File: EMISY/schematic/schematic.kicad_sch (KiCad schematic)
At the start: 6 parts

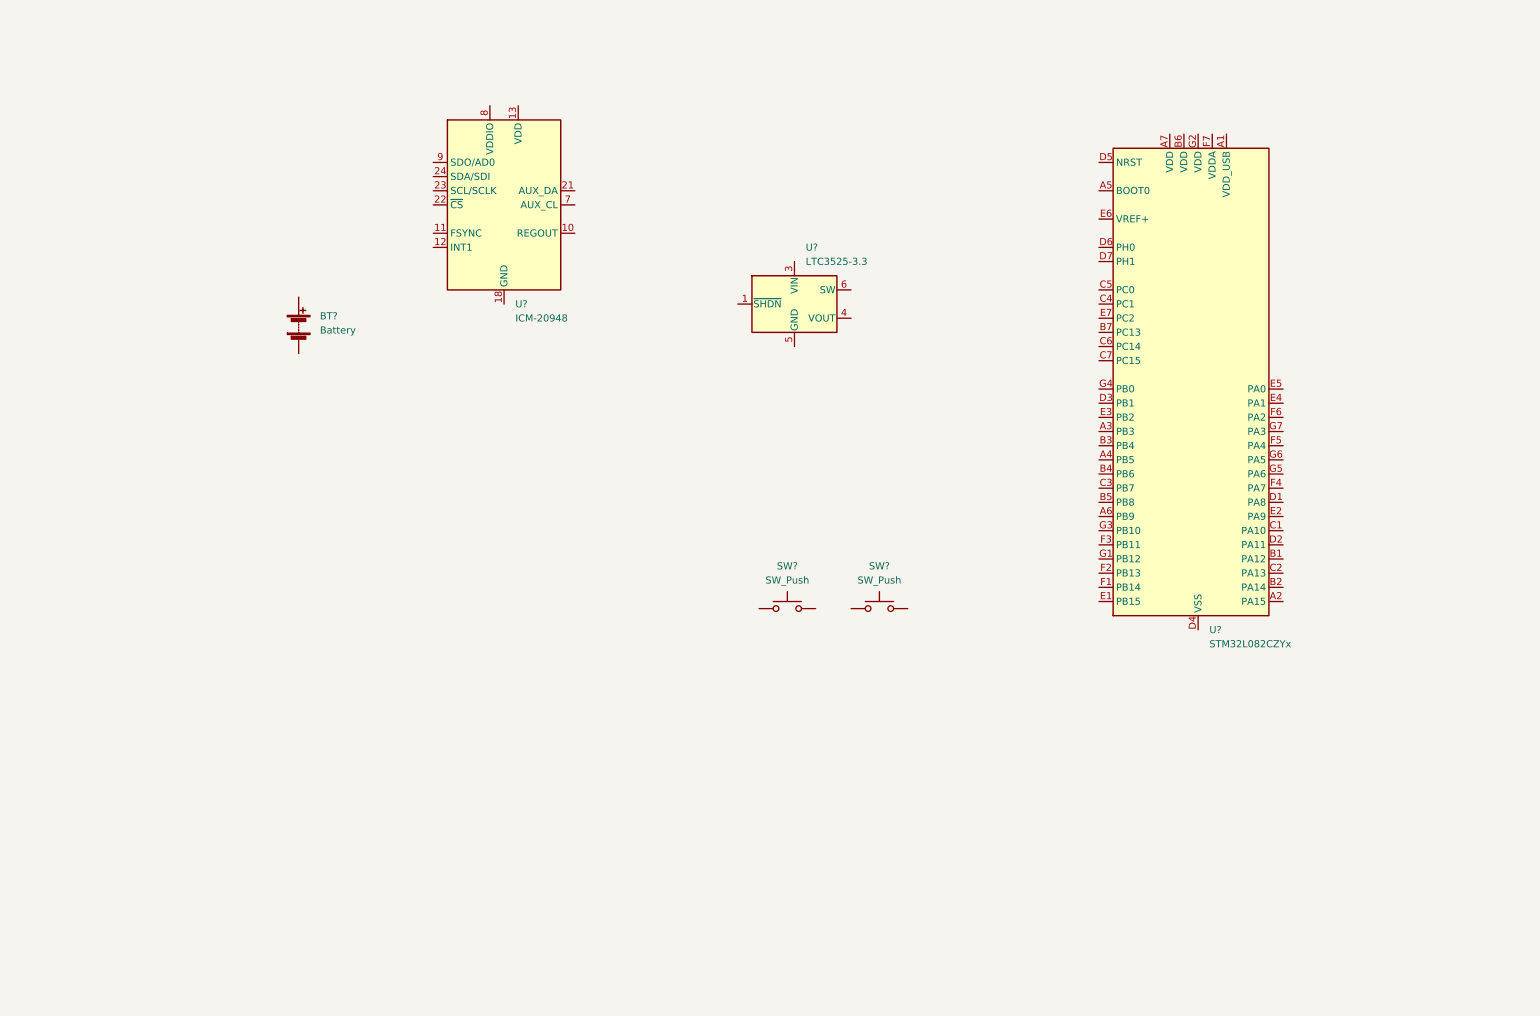
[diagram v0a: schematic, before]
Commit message: feat: add magnetometer
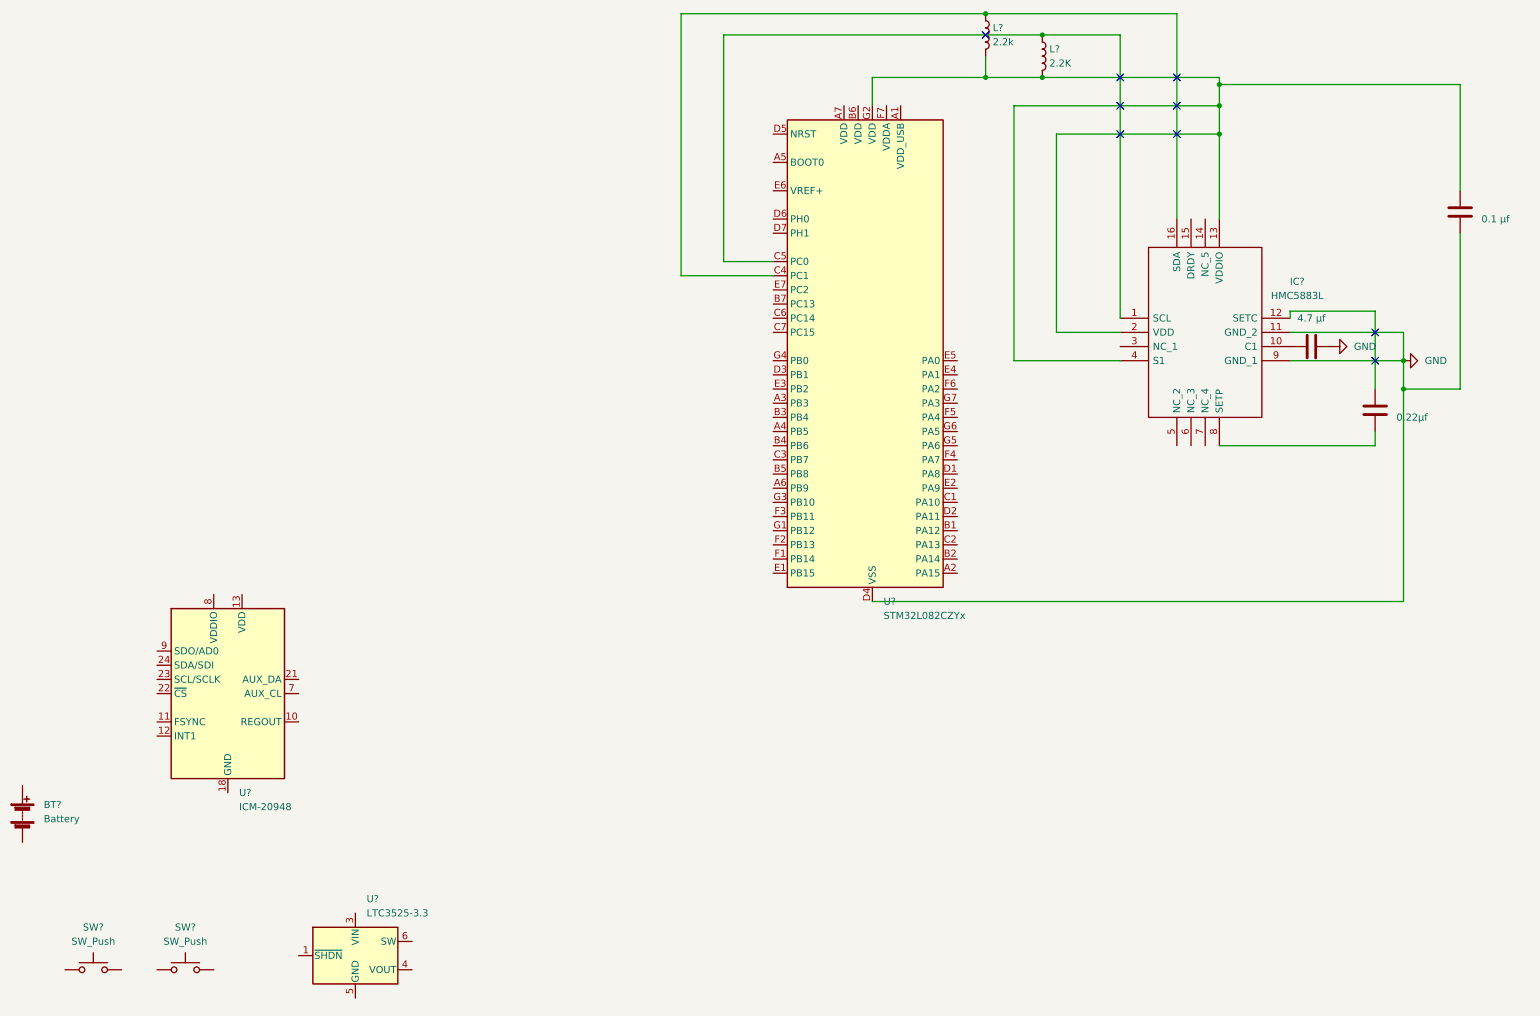
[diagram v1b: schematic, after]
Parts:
- added C?: 0.1 μf, symbol Device:C
- added C?: 4.7 μf, symbol Device:C
- added C?: 0.22μf, symbol Device:C
- added IC?: HMC5883L, HMC5883L, symbol BESTLIBRARY:HMC5883L
- added L?: 2.2K, symbol Device:L
- added L?: 2.2k, symbol Device:L
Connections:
- net at U?.C4 (PC1): now also IC?.16 (SDA), L?.1
- net at U?.C5 (PC0): now also IC?.1 (SCL), L?.1
- net GND: now reaches U?.D4 (VSS)
- net GND: now also C?.2, C?.2, IC?.11 (GND_2), IC?.9 (GND_1)
- net at U?.G2 (VDD): now also C?.1, IC?.13 (VDDIO), IC?.2 (VDD), IC?.4 (S1), L?.2, L?.2
- new net: C?.1, IC?.10 (C1)
- new net: C?.1, IC?.12 (SETC)
- new net: C?.2, IC?.8 (SETP)
- no-connect marks 0 -> 9
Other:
- moved on the sheet: BT?, SW?, U?

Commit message: feat: oled and buttons
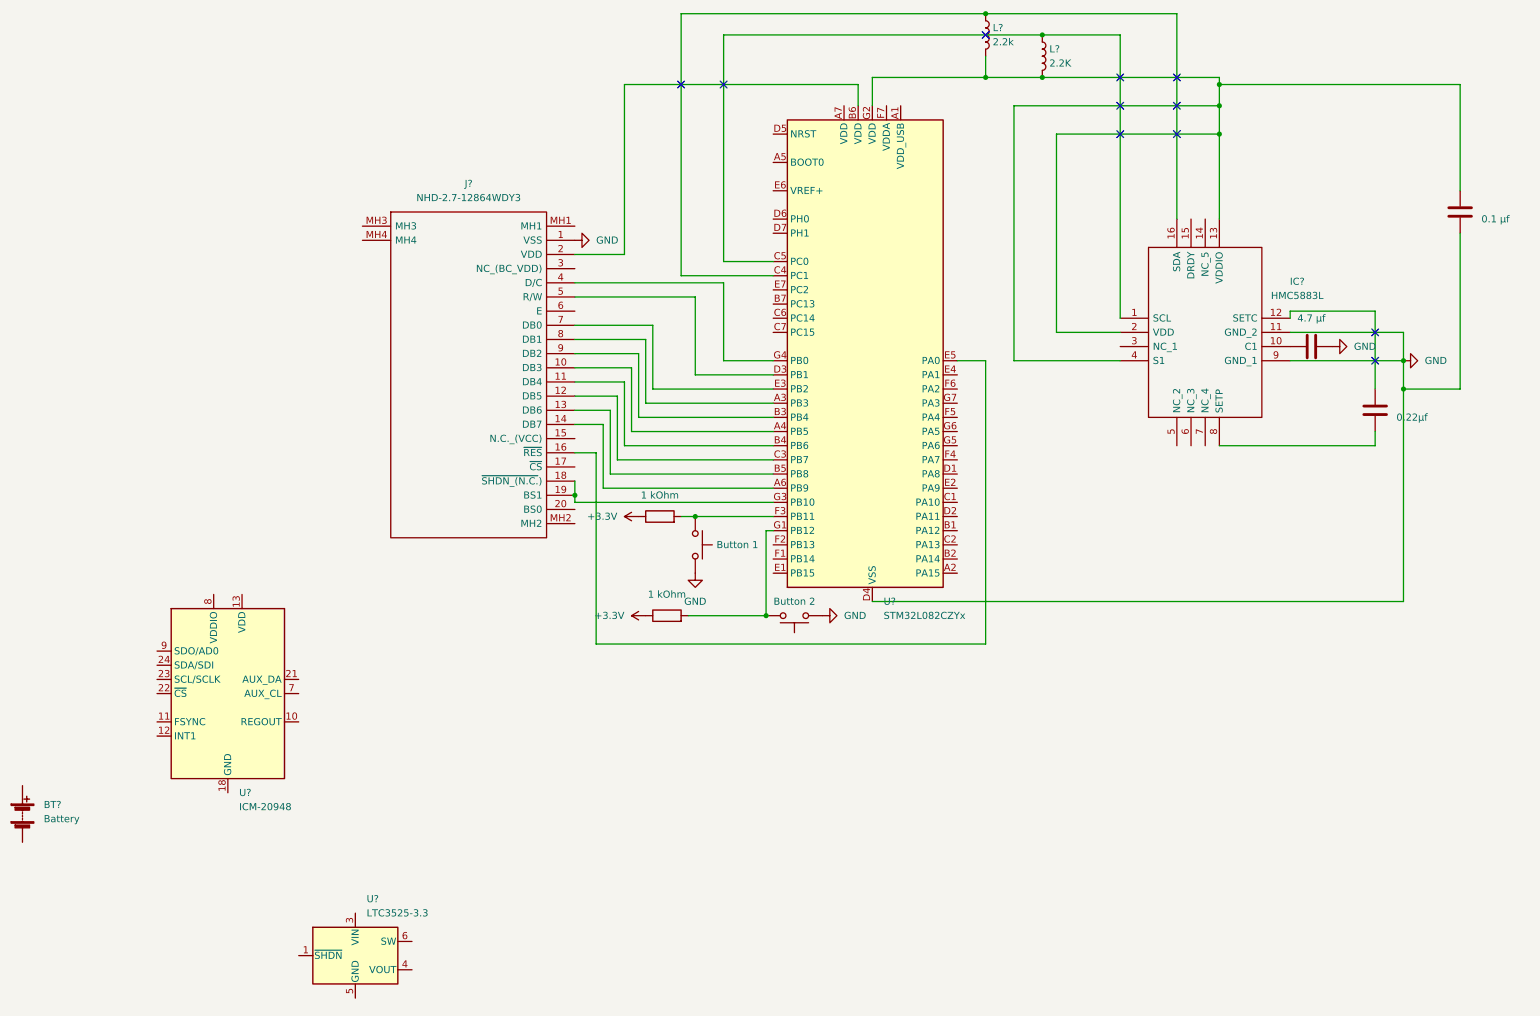
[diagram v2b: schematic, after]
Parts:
- removed SW? (x2): SW_Push, symbol Switch:SW_Push
- added J?: NHD-2.7-12864WDY3, NHD2712864WDY3, symbol BESTLIBRARY:NHD-2.7-12864WDY3
- added R? (x2): 1 kOhm, symbol Device:R
- added SW?: Button 1, symbol Switch:SW_Push
- added SW?: Button 2, symbol Switch:SW_Push
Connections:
- net GND: now also J?.1 (VSS), SW?.1, SW?.2
- net at U?.A3 (PB3): now also J?.8 (DB1)
- net at U?.A4 (PB5): now also J?.10 (DB3)
- net at U?.A6 (PB9): now also J?.14 (DB7)
- net at U?.B3 (PB4): now also J?.9 (DB2)
- net at U?.B4 (PB6): now also J?.11 (DB4)
- net at U?.B5 (PB8): now also J?.13 (DB6)
- net at U?.B6 (VDD): now also J?.2 (VDD)
- net at U?.C3 (PB7): now also J?.12 (DB5)
- net at U?.D3 (PB1): now also J?.5 (R/W)
- net at U?.E3 (PB2): now also J?.7 (DB0)
- net at U?.E5 (PA0): now also J?.16 (~{RES})
- net at U?.F3 (PB11): now also R?.2, SW?.1
- net at U?.G1 (PB12): now also R?.2, SW?.2
- net at U?.G3 (PB10): now also J?.18 (~{SHDN_(N.C.})), J?.19 (BS1)
- net at U?.G4 (PB0): now also J?.4 (D/C)
- new net +3V3: R?.1, R?.1
- no-connect marks 9 -> 11

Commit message: feat: finish schematic
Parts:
- removed U?: ICM-20948, Sensor_Motion:InvenSense_QFN-24_3x3mm_P0.4mm, symbol Sensor_Motion:ICM-20948
- added C?: 1 μF, symbol Device:C
- added C? (x2): C, symbol Device:C
- added C?: 10 μF, symbol Device:C
- added L?: 10μH, symbol Device:L
- added LR44R (x2): Battery_Cell, symbol Device:Battery_Cell
- gave numbers to parts that had none: 1
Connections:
- net +3V3: now also U?.A7 (VDD), voltageRegulator.4 (VOUT), C?.1, C?.1, C?.2
- net GND: now also voltageRegulator.2 (GND), voltageRegulator.5 (GND), C?.1, C?.2, C?.2, LR44R.2 (-)
- net 3 V: now reaches voltageRegulator.1 (~{SHDN})
- net 3 V: now also voltageRegulator.3 (VIN), C?.1, L?.1, LR44R.1 (+)
- net at voltageRegulator.6 (SW): now also L?.2
- net at U?.D5 (NRST): now also C?.2
- new net: LR44R.1 (+), LR44R.2 (-)
- no-connect marks 11 -> 13
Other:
- moved on the sheet: voltageRegulator
